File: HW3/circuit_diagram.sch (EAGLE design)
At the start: 15 parts

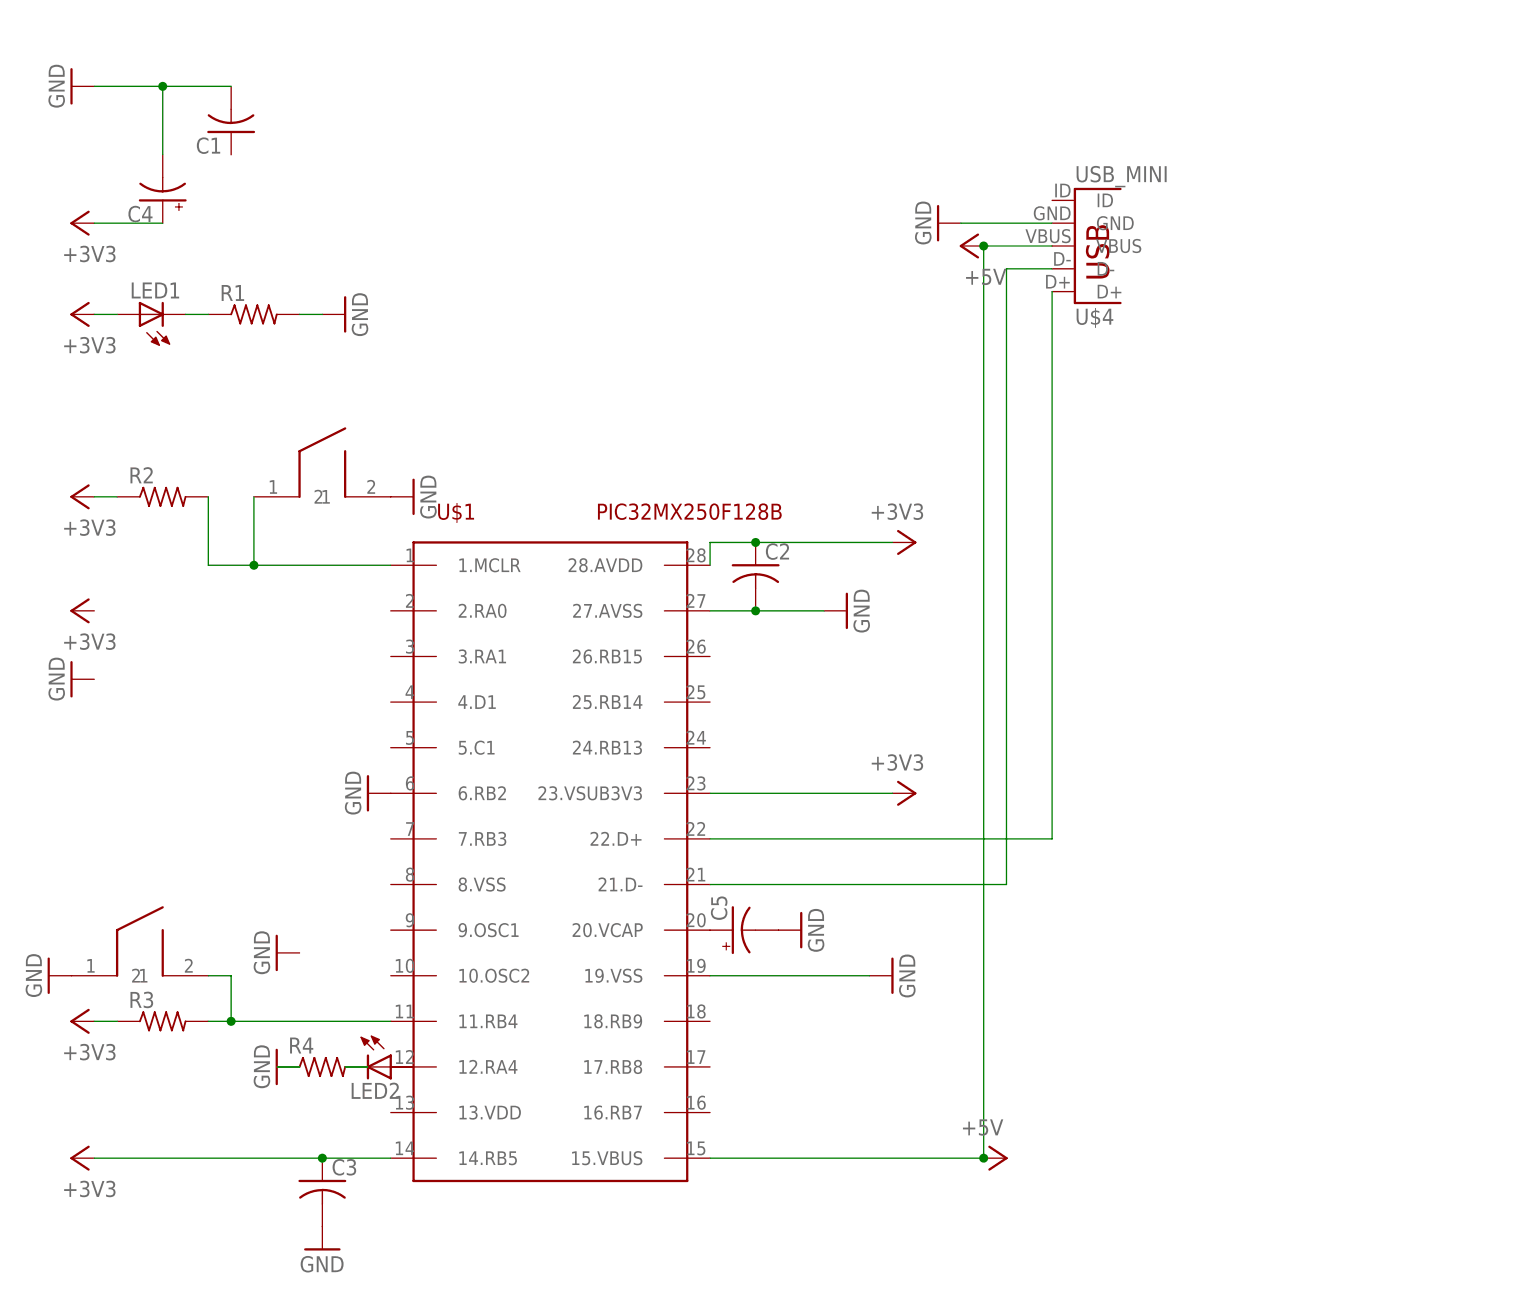
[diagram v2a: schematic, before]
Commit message: Added slide switch
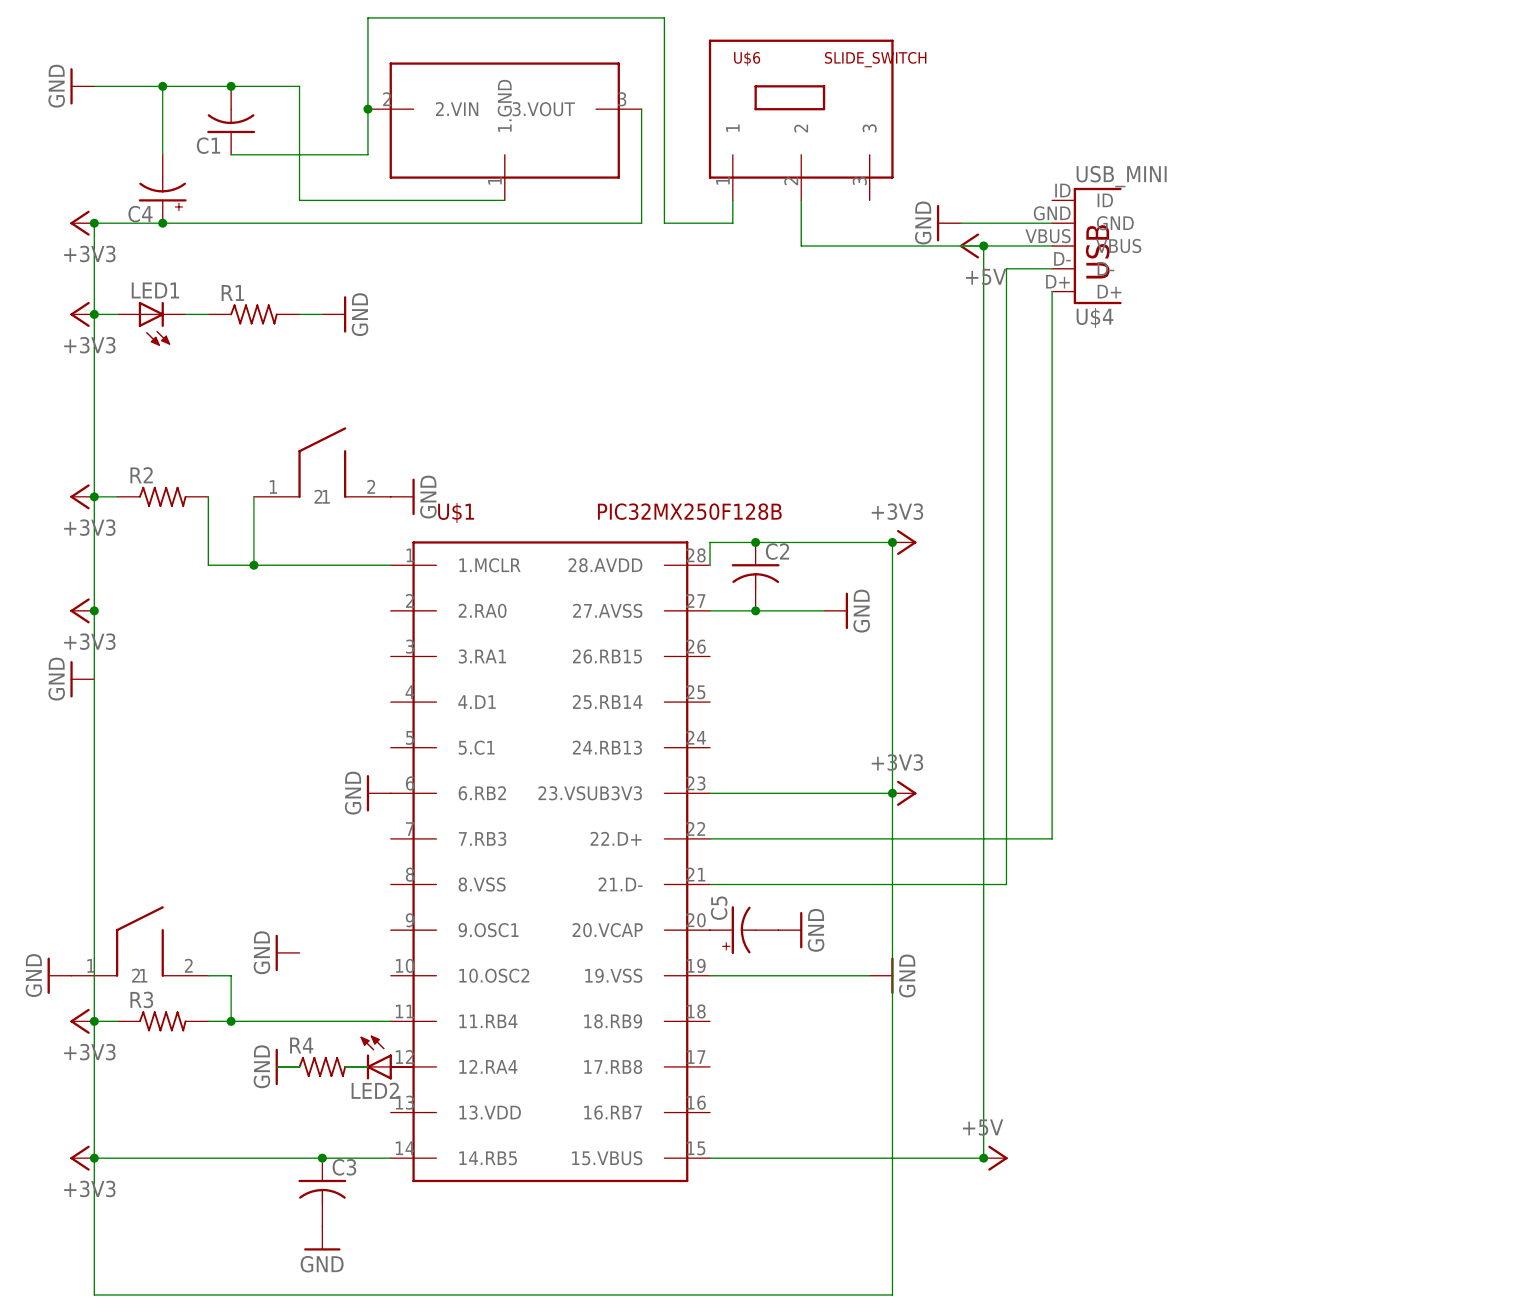
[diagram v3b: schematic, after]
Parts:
- added U$5: MCP1072, V_REG:MCP1072
- added U$6: SLIDE_SWITCH, SLIDE_SWITCH:SLIDE_SWITCH
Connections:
- new net N$8: C1.1, U$5.2.VIN, U$6.1
- net +3V3: now also U$5.3.VOUT
- net +5V: now also U$6.2
- net GND: now also U$5.1.GND
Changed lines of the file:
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@@
 <part name="U$3" library="PUSH_BUTTON" deviceset="PUSH_BUTTON_SPST-NO" device=""/>
 <part name="U$4" library="usb_conn" deviceset="USB_MINI" device=""/>
+<part name="U$5" library="V_REG" deviceset="MCP1072" device=""/>
+<part name="U$6" library="SLIDE_SWITCH" deviceset="SLIDE_SWITCH" device=""/>
 </parts>
 <sheets>
@@
 <instance part="U$3" gate="G$1" x="-35.56" y="-35.56"/>
 <instance part="U$4" gate="G$1" x="68.58" y="43.18" rot="MR180"/>
+<instance part="U$5" gate="G$1" x="5.08" y="55.88"/>
+<instance part="U$6" gate="G$1" x="38.1" y="53.34"/>
 </instances>
 <busses>
@@
 <nets>
 <net name="+3V3" class="0">
-<segment>
-<pinref part="+3V8" gate="G$1" pin="+3V3"/>
-<pinref part="C4" gate="G$1" pin="+"/>
-<wire x1="-40.64" y1="43.18" x2="-33.02" y2="43.18" width="0.1524" layer="91"/>
-</segment>
-<segment>
-<pinref part="+3V1" gate="G$1" pin="+3V3"/>
-<pinref part="LED1" gate="G$1" pin="A"/>
-<wire x1="-40.64" y1="33.02" x2="-38.1" y2="33.02" width="0.1524" layer="91"/>
-</segment>
-<segment>
-<pinref part="+3V2" gate="G$1" pin="+3V3"/>
-<pinref part="R2" gate="G$1" pin="1"/>
-<wire x1="-40.64" y1="12.7" x2="-38.1" y2="12.7" width="0.1524" layer="91"/>
-</segment>
-<segment>
-<pinref part="+3V5" gate="G$1" pin="+3V3"/>
-<pinref part="C3" gate="G$1" pin="1"/>
-<wire x1="-40.64" y1="-60.96" x2="-15.24" y2="-60.96" width="0.1524" layer="91"/>
-<pinref part="U$1" gate="G$1" pin="14.RB5"/>
-<wire x1="-15.24" y1="-60.96" x2="-7.62" y2="-60.96" width="0.1524" layer="91"/>
-<junction x="-15.24" y="-60.96"/>
-</segment>
 <segment>
 <pinref part="C2" gate="G$1" pin="1"/>
@@
 <wire x1="27.94" y1="7.62" x2="33.02" y2="7.62" width="0.1524" layer="91"/>
 <junction x="33.02" y="7.62"/>
-</segment>
-<segment>
 <pinref part="+3V4" gate="G$1" pin="+3V3"/>
 <pinref part="R3" gate="G$1" pin="1"/>
 <wire x1="-40.64" y1="-45.72" x2="-38.1" y2="-45.72" width="0.1524" layer="91"/>
-</segment>
-<segment>
+<pinref part="+3V2" gate="G$1" pin="+3V3"/>
+<pinref part="R2" gate="G$1" pin="1"/>
+<wire x1="-40.64" y1="12.7" x2="-38.1" y2="12.7" width="0.1524" layer="91"/>
+<pinref part="+3V8" gate="G$1" pin="+3V3"/>
+<pinref part="C4" gate="G$1" pin="+"/>
+<wire x1="-40.64" y1="43.18" x2="-33.02" y2="43.18" width="0.1524" layer="91"/>
+<pinref part="U$5" gate="G$1" pin="3.VOUT"/>
+<wire x1="-33.02" y1="43.18" x2="20.32" y2="43.18" width="0.1524" layer="91"/>
+<wire x1="20.32" y1="43.18" x2="20.32" y2="55.88" width="0.1524" layer="91"/>
+<junction x="-33.02" y="43.18"/>
+<pinref part="+3V1" gate="G$1" pin="+3V3"/>
+<pinref part="LED1" gate="G$1" pin="A"/>
+<wire x1="-40.64" y1="33.02" x2="-38.1" y2="33.02" width="0.1524" layer="91"/>
+<wire x1="-40.64" y1="43.18" x2="-40.64" y2="33.02" width="0.1524" layer="91"/>
+<junction x="-40.64" y="43.18"/>
+<junction x="-40.64" y="33.02"/>
+<wire x1="-40.64" y1="12.7" x2="-40.64" y2="33.02" width="0.1524" layer="91"/>
+<junction x="-40.64" y="12.7"/>
+<pinref part="+3V3" gate="G$1" pin="+3V3"/>
+<wire x1="-40.64" y1="12.7" x2="-40.64" y2="0" width="0.1524" layer="91"/>
+<wire x1="-40.64" y1="-45.72" x2="-40.64" y2="0" width="0.1524" layer="91"/>
+<junction x="-40.64" y="-45.72"/>
+<junction x="-40.64" y="0"/>
+<pinref part="+3V5" gate="G$1" pin="+3V3"/>
+<pinref part="C3" gate="G$1" pin="1"/>
+<wire x1="-40.64" y1="-60.96" x2="-15.24" y2="-60.96" width="0.1524" layer="91"/>
+<pinref part="U$1" gate="G$1" pin="14.RB5"/>
+<wire x1="-15.24" y1="-60.96" x2="-7.62" y2="-60.96" width="0.1524" layer="91"/>
+<junction x="-15.24" y="-60.96"/>
+<wire x1="-40.64" y1="-45.72" x2="-40.64" y2="-60.96" width="0.1524" layer="91"/>
+<junction x="-40.64" y="-60.96"/>
+<wire x1="-40.64" y1="-60.96" x2="-40.64" y2="-76.2" width="0.1524" layer="91"/>
 <pinref part="U$1" gate="G$1" pin="23.VSUB3V3"/>
 <pinref part="+3V7" gate="G$1" pin="+3V3"/>
 <wire x1="27.94" y1="-20.32" x2="48.26" y2="-20.32" width="0.1524" layer="91"/>
+<wire x1="-40.64" y1="-76.2" x2="48.26" y2="-76.2" width="0.1524" layer="91"/>
+<wire x1="48.26" y1="-76.2" x2="48.26" y2="-20.32" width="0.1524" layer="91"/>
+<junction x="48.26" y="-20.32"/>
+<wire x1="48.26" y1="7.62" x2="48.26" y2="-20.32" width="0.1524" layer="91"/>
+<junction x="48.26" y="7.62"/>
 </segment>
 </net>
@@
 <wire x1="-33.02" y1="58.42" x2="-25.4" y2="58.42" width="0.1524" layer="91"/>
 <junction x="-33.02" y="58.42"/>
+<wire x1="-25.4" y1="58.42" x2="-17.78" y2="58.42" width="0.1524" layer="91"/>
+<wire x1="-17.78" y1="58.42" x2="-17.78" y2="45.72" width="0.1524" layer="91"/>
+<junction x="-25.4" y="58.42"/>
+<pinref part="U$5" gate="G$1" pin="1.GND"/>
+<wire x1="-17.78" y1="45.72" x2="5.08" y2="45.72" width="0.1524" layer="91"/>
 </segment>
 <segment>
@@
 <junction x="58.42" y="40.64"/>
 <junction x="58.42" y="-60.96"/>
+<wire x1="58.42" y1="40.64" x2="38.1" y2="40.64" width="0.1524" layer="91"/>
+<pinref part="U$6" gate="G$1" pin="2"/>
+<wire x1="38.1" y1="40.64" x2="38.1" y2="45.72" width="0.1524" layer="91"/>
 </segment>
 </net>
@@
 </segment>
 </net>
+<net name="N$8" class="0">
+<segment>
+<pinref part="C1" gate="G$1" pin="1"/>
+<pinref part="U$5" gate="G$1" pin="2.VIN"/>
+<wire x1="-10.16" y1="55.88" x2="-10.16" y2="66.04" width="0.1524" layer="91"/>
+<junction x="-10.16" y="55.88"/>
+<wire x1="-10.16" y1="55.88" x2="-10.16" y2="50.8" width="0.1524" layer="91"/>
+<wire x1="-10.16" y1="50.8" x2="-25.4" y2="50.8" width="0.1524" layer="91"/>
+<pinref part="U$6" gate="G$1" pin="1"/>
+<wire x1="30.48" y1="45.72" x2="30.48" y2="43.18" width="0.1524" layer="91"/>
+<wire x1="30.48" y1="43.18" x2="22.86" y2="43.18" width="0.1524" layer="91"/>
+<wire x1="22.86" y1="43.18" x2="22.86" y2="66.04" width="0.1524" layer="91"/>
+<wire x1="22.86" y1="66.04" x2="-10.16" y2="66.04" width="0.1524" layer="91"/>
+</segment>
+</net>

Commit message: Finished schematic
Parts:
- added U$10, U$9: CONNECTOR_8PIN-HOLES, connectior-8pin-holes:CONNECTOR_8PIN-HOLES
- added U$7: OSC, OSC:OSC
- added U$8: PICKIT, pickit:PICKIT
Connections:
- new net N$10: U$1.10.OSC2, U$7.3.OSC2
- new net N$11: U$1.5.C1, U$8.5.PGC
- new net N$12: U$1.4.D1, U$8.4.PGD
- new net N$9: U$1.9.OSC1, U$7.1.OSC1
- new net RA0: U$10.1
- new net RA1: U$10.2
- new net RA4: U$10.6
- new net RB13: U$9.6
- new net RB14: U$9.7
- new net RB15: U$9.8
- new net RB2: U$10.3
- new net RB3: U$10.4
- new net RB4: U$10.5
- new net RB7: U$9.3
- new net RB8: U$9.4
- new net RB9: U$9.5
- net +3V3: now also U$10.7, U$8.2.VDD
- net +5V: now also U$9.2
- net GND: now also U$10.8, U$7.2.GND, U$8.3.GND, U$9.1
- net N$3: now also U$8.1.MCLR
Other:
- moved on the sheet: R2
